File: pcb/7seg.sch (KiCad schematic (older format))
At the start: 16 parts

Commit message: change arrangement.
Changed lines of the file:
@@
 Text Label 6450 2800 1    60   ~ 0
 KD13
-Text Notes 6350 2300 0    60   ~ 0
+Text Notes 6350 2250 0    60   ~ 0
 div number of Hz/RPM.
 Text Label 1800 3400 2    60   ~ 0

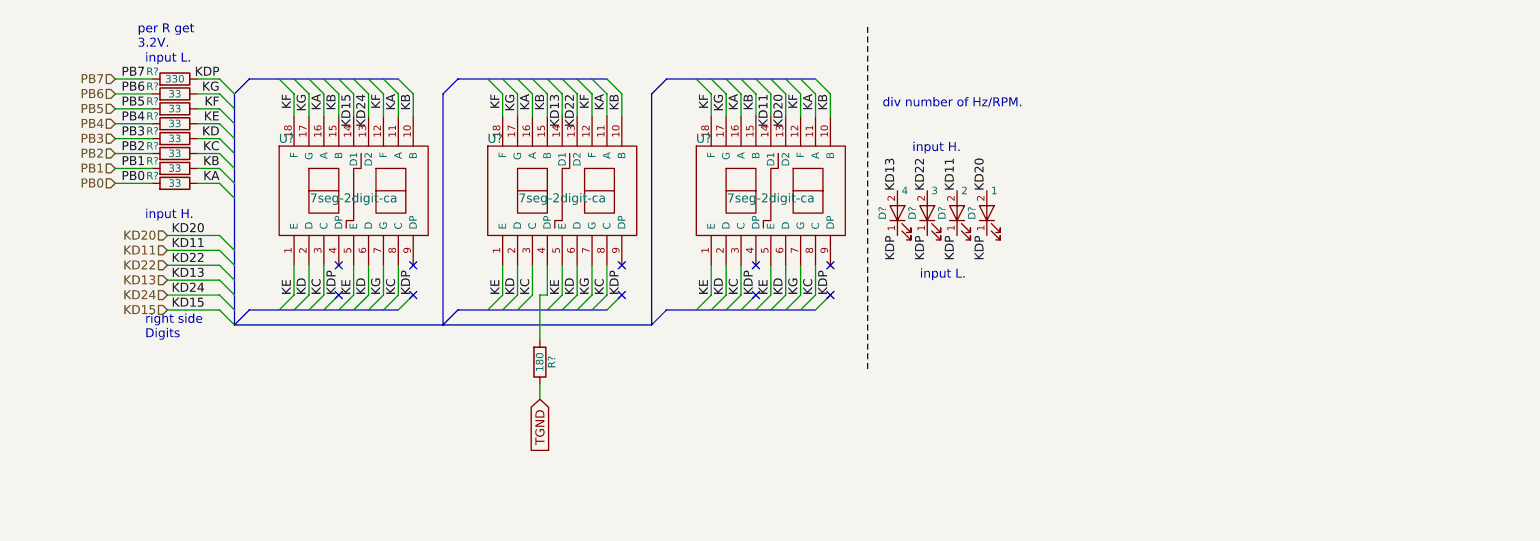
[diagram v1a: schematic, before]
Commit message: 7seg の DIG-1,2 を 2SC1815 経由で VCC と繋ぐようにした。
最初は TVCC と DIG-1,2 の接続にしていたが，7segで100mA消費すると仮定すると，
回路全体で150mA中の130mA使用する計算になり，残りの電流が20mA程度になってしまう。
なぜならば，thyristor を構成する2SA1015, 2SC1815で供給出来る電流を150mAと
計算しているから。
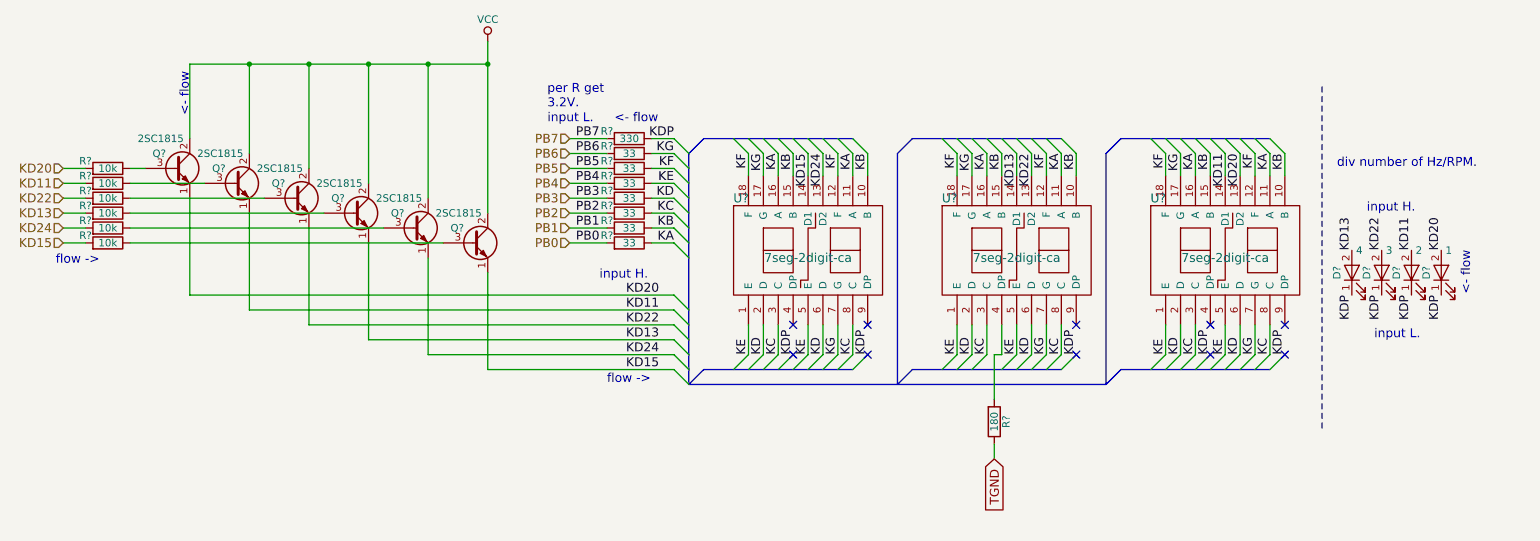
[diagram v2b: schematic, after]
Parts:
- added Q? (x6): 2SC1815, TO_SOT_Packages_THT:TO-92_Molded_Narrow, symbol 2SC1815
- added R? (x6): 10k, symbol R
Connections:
- net KD11: now also Q?.1 (E), R?.2
- net KD13: now also Q?.1 (E), R?.2
- net KD15: now also Q?.1 (E), R?.2
- net KD20: now also Q?.1 (E), R?.2
- net KD22: now also Q?.1 (E), R?.2
- net KD24: now also Q?.1 (E), R?.2
- new net: Q?.3 (B), R?.1 (x6)
- new net VCC: Q?.2 (C), Q?.2 (C), Q?.2 (C), Q?.2 (C), Q?.2 (C), Q?.2 (C)
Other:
- note added: "<- flow"
- note added: "flow ->"
- note removed: "right side\nDigits"
- moved on the sheet: D?, R?, U?

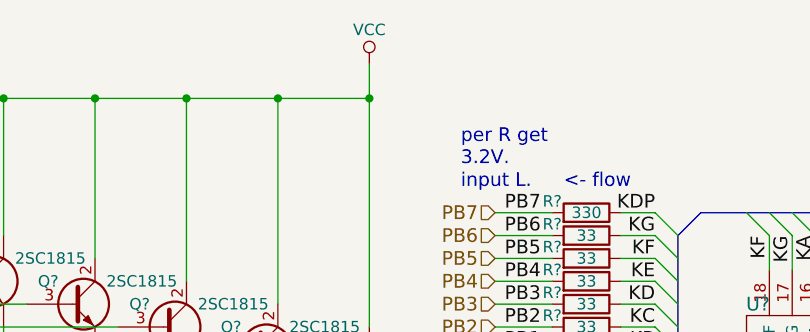
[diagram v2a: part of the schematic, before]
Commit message: 7seg sheet に TVCC を global label として設定。
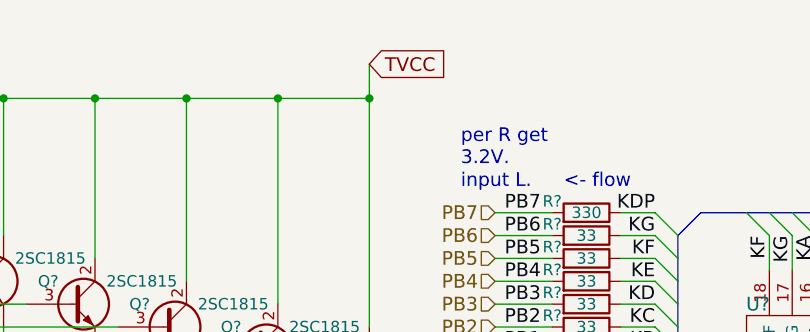
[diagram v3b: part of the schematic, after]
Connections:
- net VCC renamed TVCC
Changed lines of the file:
@@
 Connection ~ 2100 1950
 Connection ~ 3700 1950
-$Comp
-L VCC #PWR?
-U 1 1 5A10A19C
-P 3700 1800
-F 0 "#PWR?" H 3700 1650 50  0001 C CNN
-F 1 "VCC" H 3700 1950 50  0000 C CNN
-F 2 "" H 3700 1800 50  0001 C CNN
-F 3 "" H 3700 1800 50  0001 C CNN
-	1    3700 1800
-	1    0    0    -1
-$EndComp
 Text Label 4850 3700 2    60   ~ 0
 KD22
@@
 Text Notes 10300 3500 1    60   ~ 0
 <- flow
+Text GLabel 3700 1800 2    60   Input ~ 0
+TVCC
 $EndSCHEMATC

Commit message: annotate.
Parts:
- gave numbers to parts that had none: 28
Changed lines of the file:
@@
 $EndDescr
 $Comp
-L 7seg-2digit-ca U?
+L 7seg-2digit-ca U7
 U 1 1 5A12333C
 P 5850 3200
-F 0 "U?" H 5400 3550 60  0000 C CNN
+F 0 "U7" H 5400 3550 60  0000 C CNN
 F 1 "7seg-2digit-ca" H 5850 3150 60  0000 C CNN
 F 2 "" H 6100 3300 60  0001 C CNN
@@
 	5050 4100 5150 4000
 $Comp
-L R R?
+L R R39
 U 1 1 5A123365
 P 4650 2550
-F 0 "R?" V 4700 2400 50  0000 C CNN
+F 0 "R39" V 4700 2400 50  0000 C CNN
 F 1 "33" V 4650 2550 50  0000 C CNN
 F 2 "" V 4580 2550 50  0001 C CNN
@@
 $EndComp
 $Comp
-L R R?
+L R R40
 U 1 1 5A12336C
 P 4650 2650
-F 0 "R?" V 4700 2500 50  0000 C CNN
+F 0 "R40" V 4700 2500 50  0000 C CNN
 F 1 "33" V 4650 2650 50  0000 C CNN
 F 2 "" V 4580 2650 50  0001 C CNN
@@
 $EndComp
 $Comp
-L R R?
+L R R41
 U 1 1 5A123373
 P 4650 2750
-F 0 "R?" V 4700 2600 50  0000 C CNN
+F 0 "R41" V 4700 2600 50  0000 C CNN
 F 1 "33" V 4650 2750 50  0000 C CNN
 F 2 "" V 4580 2750 50  0001 C CNN
@@
 $EndComp
 $Comp
-L R R?
+L R R42
 U 1 1 5A12337A
 P 4650 2850
-F 0 "R?" V 4700 2700 50  0000 C CNN
+F 0 "R42" V 4700 2700 50  0000 C CNN
 F 1 "33" V 4650 2850 50  0000 C CNN
 F 2 "" V 4580 2850 50  0001 C CNN
@@
 $EndComp
 $Comp
-L R R?
+L R R43
 U 1 1 5A123381
 P 4650 2950
-F 0 "R?" V 4700 2800 50  0000 C CNN
+F 0 "R43" V 4700 2800 50  0000 C CNN
 F 1 "33" V 4650 2950 50  0000 C CNN
 F 2 "" V 4580 2950 50  0001 C CNN
@@
 $EndComp
 $Comp
-L R R?
+L R R44
 U 1 1 5A123388
 P 4650 3050
-F 0 "R?" V 4700 2900 50  0000 C CNN
+F 0 "R44" V 4700 2900 50  0000 C CNN
 F 1 "33" V 4650 3050 50  0000 C CNN
 F 2 "" V 4580 3050 50  0001 C CNN
@@
 $EndComp
 $Comp
-L R R?
+L R R45
 U 1 1 5A12338F
 P 4650 3150
-F 0 "R?" V 4700 3000 50  0000 C CNN
+F 0 "R45" V 4700 3000 50  0000 C CNN
 F 1 "33" V 4650 3150 50  0000 C CNN
 F 2 "" V 4580 3150 50  0001 C CNN
@@
 	5050 3250 4950 3150
 $Comp
-L 7seg-2digit-ca U?
+L 7seg-2digit-ca U8
 U 1 1 5A1233A6
 P 7250 3200
-F 0 "U?" H 6800 3550 60  0000 C CNN
+F 0 "U8" H 6800 3550 60  0000 C CNN
 F 1 "7seg-2digit-ca" H 7250 3150 60  0000 C CNN
 F 2 "" H 7500 3300 60  0001 C CNN
@@
 	6450 4100 6550 4000
 $Comp
-L 7seg-2digit-ca U?
+L 7seg-2digit-ca U9
 U 1 1 5A1233CF
 P 8650 3200
-F 0 "U?" H 8200 3550 60  0000 C CNN
+F 0 "U9" H 8200 3550 60  0000 C CNN
 F 1 "7seg-2digit-ca" H 8650 3150 60  0000 C CNN
 F 2 "" H 8900 3300 60  0001 C CNN
@@
 NoConn ~ 7650 3700
 $Comp
-L LED D?
+L LED D8
 U 1 1 5A123402
 P 9700 3350
-F 0 "D?" H 9700 3450 50  0000 C CNN
+F 0 "D8" H 9700 3450 50  0000 C CNN
 F 1 "3" V 9850 3300 50  0000 C CNN
 F 2 "" H 9700 3350 50  0001 C CNN
@@
 $EndComp
 $Comp
-L LED D?
+L LED D9
 U 1 1 5A123409
 P 9900 3350
-F 0 "D?" H 9900 3450 50  0000 C CNN
+F 0 "D9" H 9900 3450 50  0000 C CNN
 F 1 "2" V 10050 3300 50  0000 C CNN
 F 2 "" H 9900 3350 50  0001 C CNN
@@
 $EndComp
 $Comp
-L LED D?
+L LED D7
 U 1 1 5A123410
 P 9500 3350
-F 0 "D?" H 9500 3450 50  0000 C CNN
+F 0 "D7" H 9500 3450 50  0000 C CNN
 F 1 "4" V 9650 3300 50  0000 C CNN
 F 2 "" H 9500 3350 50  0001 C CNN
@@
 $EndComp
 $Comp
-L LED D?
+L LED D10
 U 1 1 5A123417
 P 10100 3350
-F 0 "D?" H 10100 3450 50  0000 C CNN
+F 0 "D10" H 10100 3450 50  0000 C CNN
 F 1 "1" V 10250 3300 50  0000 C CNN
 F 2 "" H 10100 3350 50  0001 C CNN
@@
 KDP
 $Comp
-L R R?
+L R R46
 U 1 1 5A123422
 P 7100 4350
-F 0 "R?" V 7180 4350 50  0000 C CNN
+F 0 "R46" V 7180 4350 50  0000 C CNN
 F 1 "180" V 7100 4350 50  0000 C CNN
 F 2 "" V 7030 4350 50  0001 C CNN
@@
 KD15
 $Comp
-L R R?
+L R R38
 U 1 1 5A129408
 P 4650 2450
-F 0 "R?" V 4700 2300 50  0000 C CNN
+F 0 "R38" V 4700 2300 50  0000 C CNN
 F 1 "330" V 4650 2450 50  0000 C CNN
 F 2 "" V 4580 2450 50  0001 C CNN
@@
 TGND
 $Comp
-L 2SC1815 Q?
+L 2SC1815 Q9
 U 1 1 5A107034
 P 1600 2650
-F 0 "Q?" H 1450 2750 50  0000 L CNN
+F 0 "Q9" H 1450 2750 50  0000 L CNN
 F 1 "2SC1815" H 1350 2850 50  0000 L CNN
 F 2 "TO_SOT_Packages_THT:TO-92_Molded_Narrow" H 1800 2575 50  0001 L CIN
@@
 $EndComp
 $Comp
-L R R?
+L R R32
 U 1 1 5A1075D9
 P 1150 2650
-F 0 "R?" V 1200 2500 50  0000 C CNN
+F 0 "R32" V 1200 2500 50  0000 C CNN
 F 1 "10k" V 1150 2650 50  0000 C CNN
 F 2 "" V 1080 2650 50  0001 C CNN
@@
 $EndComp
 $Comp
-L R R?
+L R R33
 U 1 1 5A107776
 P 1150 2750
-F 0 "R?" V 1200 2600 50  0000 C CNN
+F 0 "R33" V 1200 2600 50  0000 C CNN
 F 1 "10k" V 1150 2750 50  0000 C CNN
 F 2 "" V 1080 2750 50  0001 C CNN
@@
 $EndComp
 $Comp
-L R R?
+L R R34
 U 1 1 5A1077BF
 P 1150 2850
-F 0 "R?" V 1200 2700 50  0000 C CNN
+F 0 "R34" V 1200 2700 50  0000 C CNN
 F 1 "10k" V 1150 2850 50  0000 C CNN
 F 2 "" V 1080 2850 50  0001 C CNN
@@
 $EndComp
 $Comp
-L R R?
+L R R35
 U 1 1 5A10780B
 P 1150 2950
-F 0 "R?" V 1200 2800 50  0000 C CNN
+F 0 "R35" V 1200 2800 50  0000 C CNN
 F 1 "10k" V 1150 2950 50  0000 C CNN
 F 2 "" V 1080 2950 50  0001 C CNN
@@
 $EndComp
 $Comp
-L R R?
+L R R36
 U 1 1 5A10785A
 P 1150 3050
-F 0 "R?" V 1200 2900 50  0000 C CNN
+F 0 "R36" V 1200 2900 50  0000 C CNN
 F 1 "10k" V 1150 3050 50  0000 C CNN
 F 2 "" V 1080 3050 50  0001 C CNN
@@
 $EndComp
 $Comp
-L R R?
+L R R37
 U 1 1 5A1078AC
 P 1150 3150
-F 0 "R?" V 1200 3000 50  0000 C CNN
+F 0 "R37" V 1200 3000 50  0000 C CNN
 F 1 "10k" V 1150 3150 50  0000 C CNN
 F 2 "" V 1080 3150 50  0001 C CNN
@@
 $EndComp
 $Comp
-L 2SC1815 Q?
+L 2SC1815 Q10
 U 1 1 5A107D1F
 P 2000 2750
-F 0 "Q?" H 1850 2850 50  0000 L CNN
+F 0 "Q10" H 1850 2850 50  0000 L CNN
 F 1 "2SC1815" H 1750 2950 50  0000 L CNN
 F 2 "TO_SOT_Packages_THT:TO-92_Molded_Narrow" H 2200 2675 50  0001 L CIN
@@
 $EndComp
 $Comp
-L 2SC1815 Q?
+L 2SC1815 Q11
 U 1 1 5A107D99
 P 2400 2850
-F 0 "Q?" H 2250 2950 50  0000 L CNN
+F 0 "Q11" H 2250 2950 50  0000 L CNN
 F 1 "2SC1815" H 2150 3050 50  0000 L CNN
 F 2 "TO_SOT_Packages_THT:TO-92_Molded_Narrow" H 2600 2775 50  0001 L CIN
@@
 $EndComp
 $Comp
-L 2SC1815 Q?
+L 2SC1815 Q12
 U 1 1 5A107E06
 P 2800 2950
-F 0 "Q?" H 2650 3050 50  0000 L CNN
+F 0 "Q12" H 2650 3050 50  0000 L CNN
 F 1 "2SC1815" H 2550 3150 50  0000 L CNN
 F 2 "TO_SOT_Packages_THT:TO-92_Molded_Narrow" H 3000 2875 50  0001 L CIN
@@
 $EndComp
 $Comp
-L 2SC1815 Q?
+L 2SC1815 Q13
 U 1 1 5A107E72
 P 3200 3050
-F 0 "Q?" H 3050 3150 50  0000 L CNN
+F 0 "Q13" H 3050 3150 50  0000 L CNN
 F 1 "2SC1815" H 2950 3250 50  0000 L CNN
 F 2 "TO_SOT_Packages_THT:TO-92_Molded_Narrow" H 3400 2975 50  0001 L CIN
@@
 $EndComp
 $Comp
-L 2SC1815 Q?
+L 2SC1815 Q14
 U 1 1 5A107FF8
 P 3600 3150
-F 0 "Q?" H 3450 3250 50  0000 L CNN
+F 0 "Q14" H 3450 3250 50  0000 L CNN
 F 1 "2SC1815" H 3350 3350 50  0000 L CNN
 F 2 "TO_SOT_Packages_THT:TO-92_Molded_Narrow" H 3800 3075 50  0001 L CIN
